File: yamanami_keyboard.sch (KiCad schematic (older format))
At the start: 148 parts, among them J1 Breakaway_Tabs, J10 Conn_01x04, J11 Breakaway_Tabs, J12 Breakaway_Tabs, J13 Breakaway_Tabs, J14 Breakaway_Tabs, J2 Breakaway_Tabs, J3 Breakaway_Tabs, J4 Breakaway_Tabs, J5 Conn_02x03_Odd_Even, J6 USB_C_Receptacle_USB2.0, J7 Conn_01x04, J8 Conn_02x03_Odd_Even, J9 USB_C_Receptacle_USB2.0, SW1 SW_Push, SW2 SW_Push, U1 ATmega32U4-AU, U2 PRTR5V0U2X, U3 ATmega32U4-AU, U4 PRTR5V0U2X, Y1 16MHz, Y2 16MHz

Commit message: fixed symbol.
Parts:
- C1, C10, C11, C12, C13, C18, C2, C3, C4, C5, C7, C8, C9: symbol arch_keyboard-rescue:C_Small-Device -> Device:C_Small
- C15: symbol yamanami_keyboard-rescue:C_Small-Device -> Device:C_Small
- D1, D10, D11, D12, D13, D14, D15, D16, D17, D18, D19, D2, D20, D21, D22, D23, D24, D25, D26, D27, D28, D29, D3, D30, D31, D32, D33, D34, D35, D36, D37, D38, D39, D4, D40, D41, D42, D43, D44, D45, D46, D47, D48, D5, D6, D7, D8, D9: symbol yamanami_keyboard-rescue:D_Small-Device -> Device:D_Small
- D49, D50: symbol yamanami_keyboard-rescue:D_Schottky_Small-Device -> Device:D_Schottky_Small
- F1, F2: symbol yamanami_keyboard-rescue:Polyfuse-Device -> Device:Polyfuse
- J1, J11, J12, J13, J14, J2, J3, J4: symbol yamanami_keyboard-rescue:Conn_01x01-Connector_Generic -> Connector_Generic:Conn_01x01
- J10, J7: symbol yamanami_keyboard-rescue:Conn_01x04-Connector_Generic -> Connector_Generic:Conn_01x04
- J5: symbol arch_keyboard-rescue:Conn_02x03_Odd_Even-Connector_Generic -> Connector_Generic:Conn_02x03_Odd_Even
- J8: symbol yamanami_keyboard-rescue:Conn_02x03_Odd_Even-Connector_Generic -> Connector_Generic:Conn_02x03_Odd_Even
- R10, R11, R12, R2, R3, R5, R6, R9: symbol arch_keyboard-rescue:R-Device -> Device:R
- R7: symbol yamanami_keyboard-rescue:R-Device -> Device:R
- U1, U3: symbol yamanami_keyboard-rescue:ATmega32U4-AU-MCU_Microchip_ATmega -> MCU_Microchip_ATmega:ATmega32U4-AU
- Y1, Y2: symbol arch_keyboard-rescue:Crystal_GND24-Device -> Device:Crystal_GND24
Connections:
- wire segments 367 -> 365

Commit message: 間違い修正
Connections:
- wire segments 365 -> 370
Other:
- moved on the sheet: C1, C10, C2, C9, D49, F1, R5, R6, R7, SW1, SW2, U2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

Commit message: 大改修前の保存
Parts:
- added J15, J16, J19, J20: Conn_01x01, Connector_Pin:Pin_D1.0mm_L10.0mm, symbol Connector_Generic:Conn_01x01
- R1: symbol yamanami_keyboard-rescue:R-Device -> yamanami_keyboard-rescue:R-Device-yamanami_keyboard-rescue
- R4, R8: symbol arch_keyboard-rescue:R-Device -> yamanami_keyboard-rescue:R-Device-arch_keyboard-rescue
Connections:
- net labels added: reserve1, reserve1_R, reserve2, reserve2_R
- wire segments 370 -> 384
- no-connect marks 38 -> 34
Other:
- note added: "Mousebite"
- note added: "Reserve_pin"
- moved on the sheet: C10, C11, C12, C13, C15, C18, C9, D1, D10, D11, D12, D13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

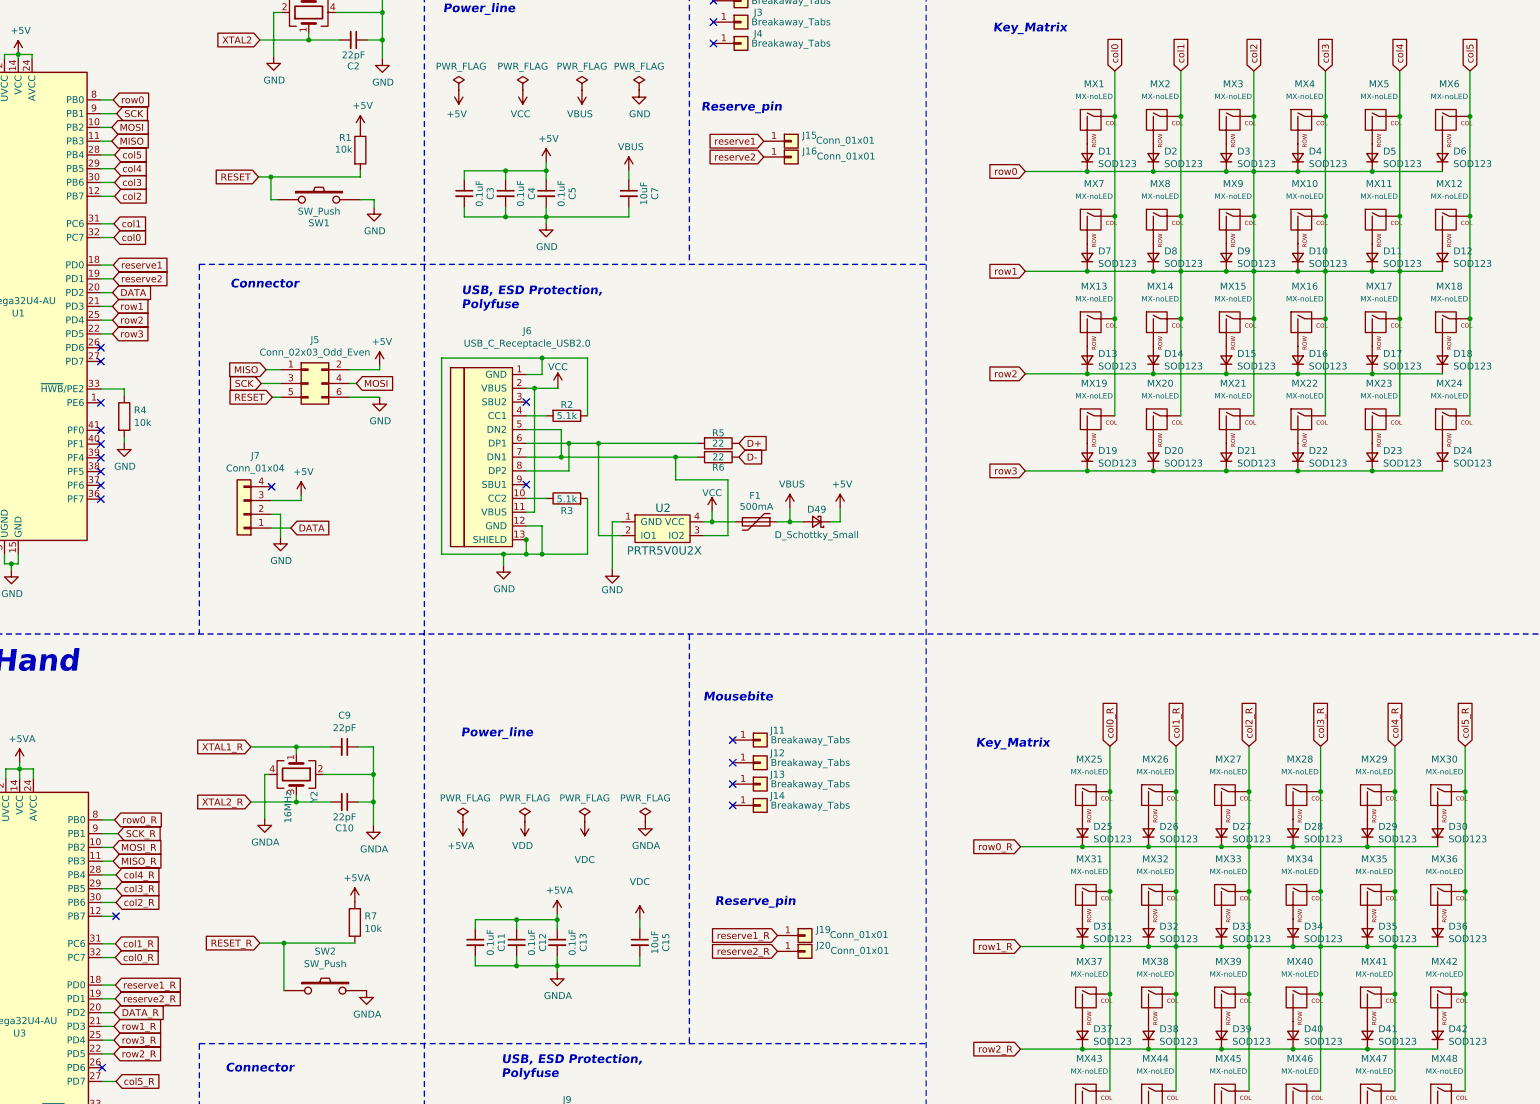
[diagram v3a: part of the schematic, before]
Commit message: 左手の配線ほぼ完了
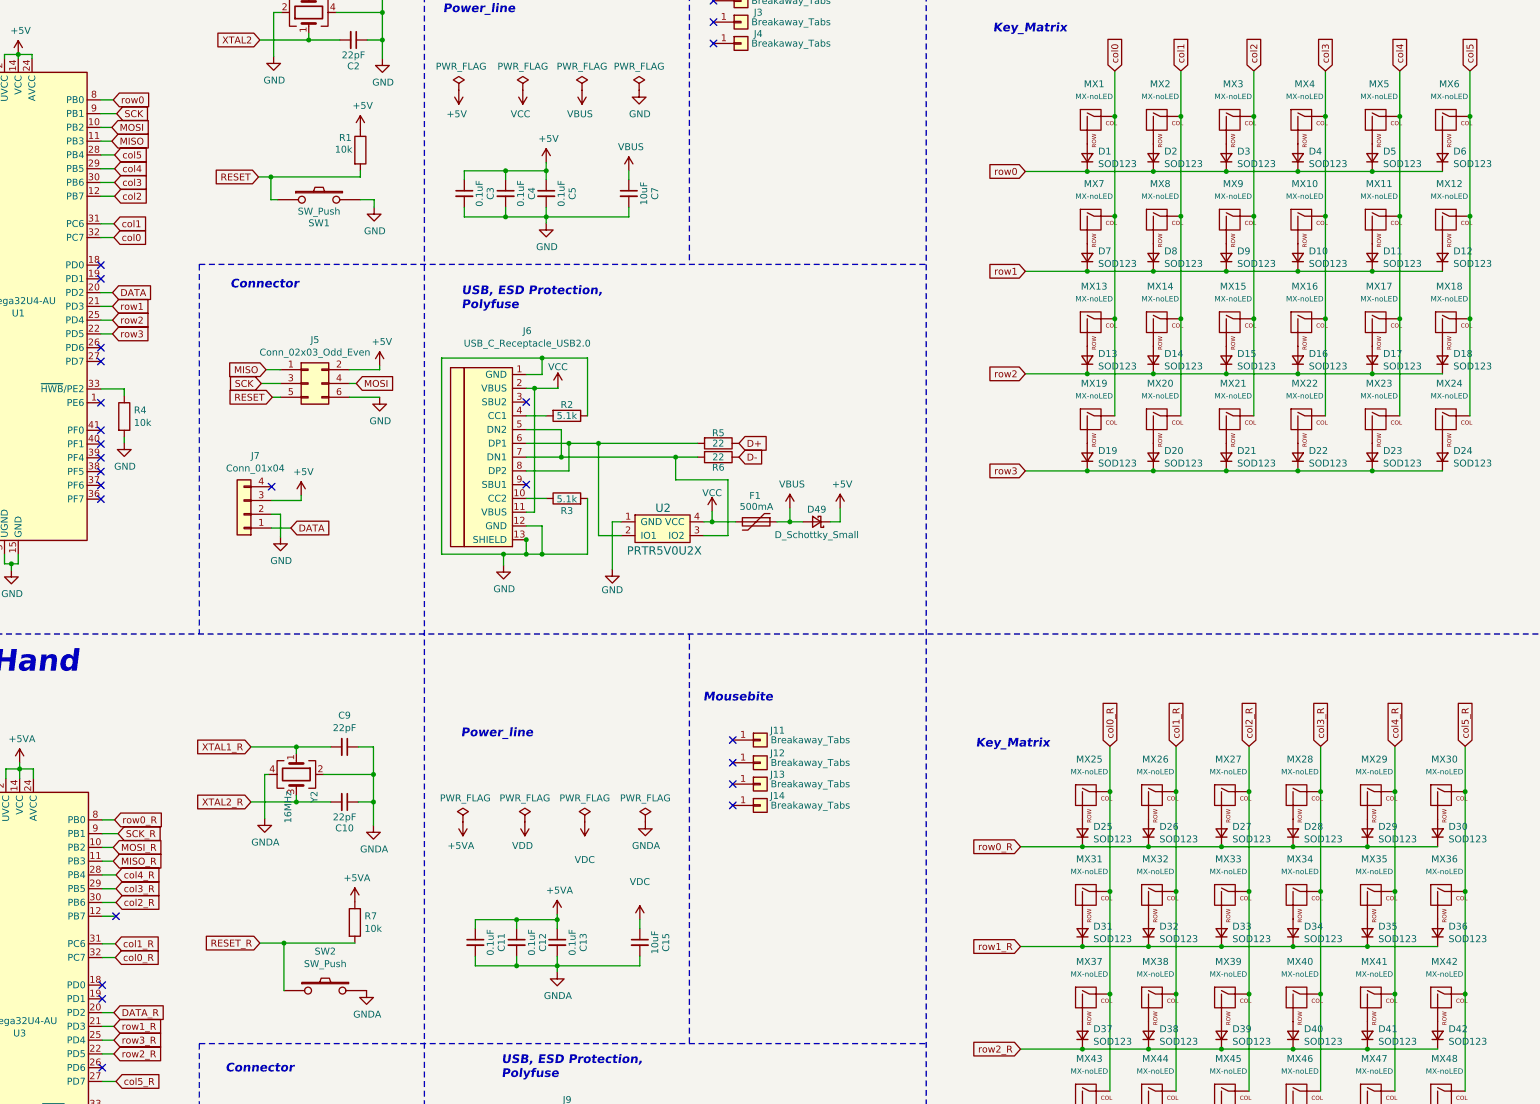
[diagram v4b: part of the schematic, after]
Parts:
- removed J15, J16, J19, J20: Conn_01x01, Connector_Pin:Pin_D1.0mm_L10.0mm, symbol Connector_Generic:Conn_01x01
- R1, R10, R11, R12, R2, R3, R4, R5, R6, R7, R8, R9: footprint Resistor_SMD:R_0805_2012Metric -> Resistor_SMD:R_0603_1608Metric
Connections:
- net col1: no longer D1.1 (K), D10.1 (K), D11.1 (K), D12.1 (K), D2.1 (K), D3.1 (K), D4.1 (K), D5.1 (K), D6.1 (K), D7.1 (K), D8.1 (K), D9.1 (K), MX10.1 (COL), MX11.1 (COL), MX15.1 (COL), MX16.1 (COL), MX17.1 (COL), MX21.1 (COL), MX22.1 (COL), MX23.1 (COL), MX3.1 (COL), MX4.1 (COL), MX5.1 (COL), MX9.1 (COL), U1.12 (PB7), U1.21 (PD3), U1.29 (PB5), U1.30 (PB6), U1.8 (PB0)
- net col1_R: no longer D25.1 (K), D26.1 (K), D27.1 (K), D28.1 (K), D29.1 (K), D30.1 (K), D31.1 (K), D32.1 (K), D33.1 (K), D34.1 (K), D35.1 (K), D36.1 (K), MX27.1 (COL), MX28.1 (COL), MX29.1 (COL), MX33.1 (COL), MX34.1 (COL), MX35.1 (COL), MX39.1 (COL), MX40.1 (COL), MX41.1 (COL), MX45.1 (COL), MX46.1 (COL), MX47.1 (COL), U3.21 (PD3), U3.28 (PB4), U3.29 (PB5), U3.30 (PB6), U3.8 (PB0)
- net reserve1: no longer names the net of U1.18 (PD0)
- net reserve1_R: no longer names the net of U3.18 (PD0)
- net reserve2: no longer names the net of U1.19 (PD1)
- net reserve2_R: no longer names the net of U3.19 (PD1)
- new net col2: MX15.1 (COL), MX21.1 (COL), MX3.1 (COL), MX9.1 (COL), U1.12 (PB7)
- new net col2_R: MX27.1 (COL), MX33.1 (COL), MX39.1 (COL), MX45.1 (COL), U3.30 (PB6)
- new net col3: MX10.1 (COL), MX16.1 (COL), MX22.1 (COL), MX4.1 (COL), U1.30 (PB6)
- new net col3_R: MX28.1 (COL), MX34.1 (COL), MX40.1 (COL), MX46.1 (COL), U3.29 (PB5)
- new net col4: MX11.1 (COL), MX17.1 (COL), MX23.1 (COL), MX5.1 (COL), U1.29 (PB5)
- new net col4_R: MX29.1 (COL), MX35.1 (COL), MX41.1 (COL), MX47.1 (COL), U3.28 (PB4)
- new net row0: D1.1 (K), D2.1 (K), D3.1 (K), D4.1 (K), D5.1 (K), D6.1 (K), U1.8 (PB0)
- new net row0_R: D25.1 (K), D26.1 (K), D27.1 (K), D28.1 (K), D29.1 (K), D30.1 (K), U3.8 (PB0)
- new net row1: D10.1 (K), D11.1 (K), D12.1 (K), D7.1 (K), D8.1 (K), D9.1 (K), U1.21 (PD3)
- new net row1_R: D31.1 (K), D32.1 (K), D33.1 (K), D34.1 (K), D35.1 (K), D36.1 (K), U3.21 (PD3)
- no-connect marks 34 -> 38
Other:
- note removed: "Reserve_pin"
